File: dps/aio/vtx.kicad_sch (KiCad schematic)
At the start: 14 parts, among them J201 HD VTX, U201 LMR51430YFDDCR

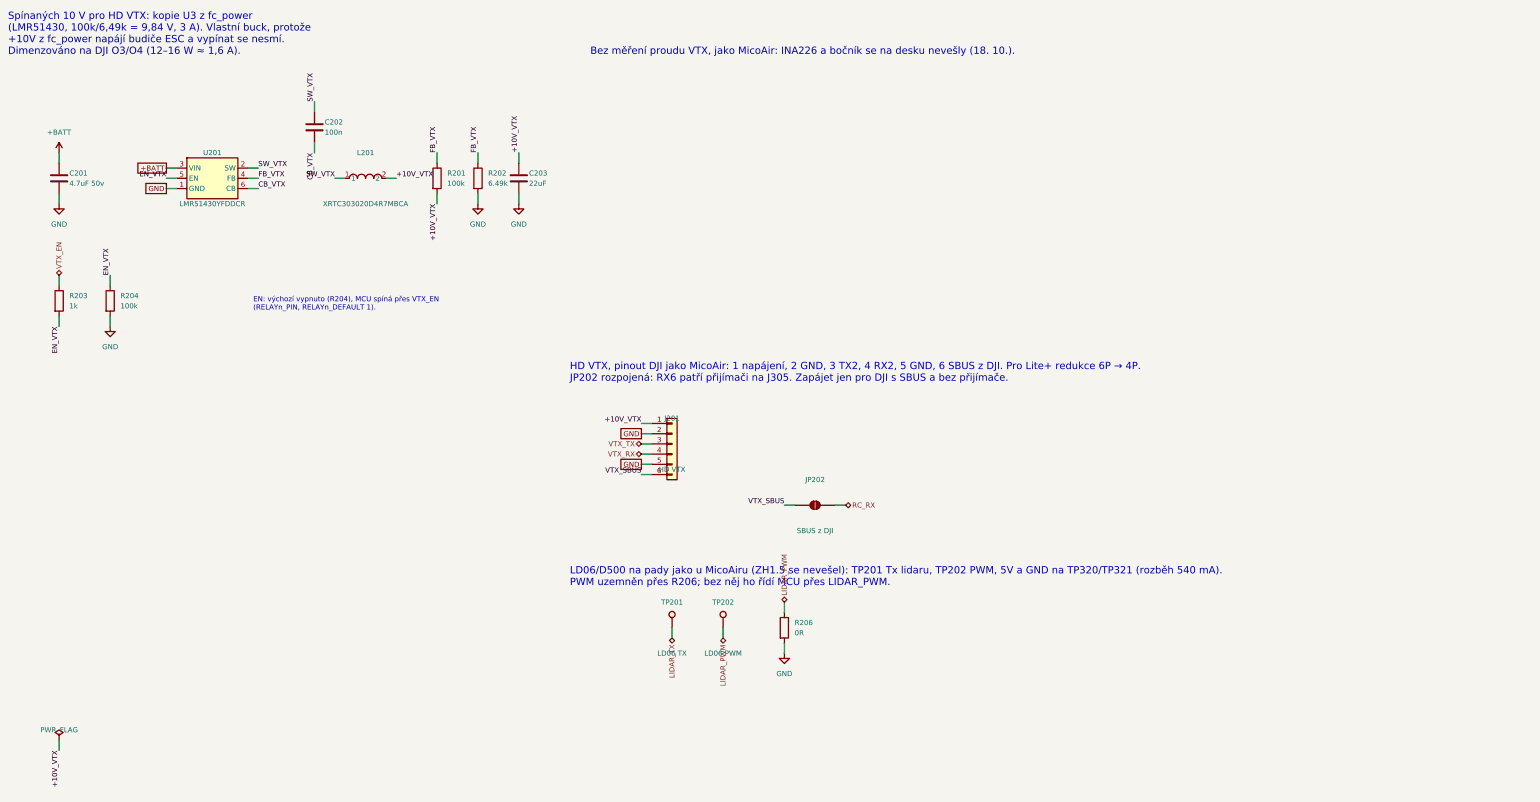
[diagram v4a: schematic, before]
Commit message: feat: fit every AIO part on the board: switch the VTX off +10V and take an ICM-42688-P as the second IMU
The VTX buck and the BMI088 did not fit; the largest free spot was 2.5 x 2.9 mm.
The VTX now hangs on fc_power's +10V behind a TPS22810 load switch (as OpenAIO
feeds it, but switchable), and the second IMU is an ICM-42688-P on OpenAIO's
LGA-14 footprint. The board update now also carries values and LCSC numbers.

Co-Authored-By: Claude Opus 5.5 <noreply@anthropic.com>
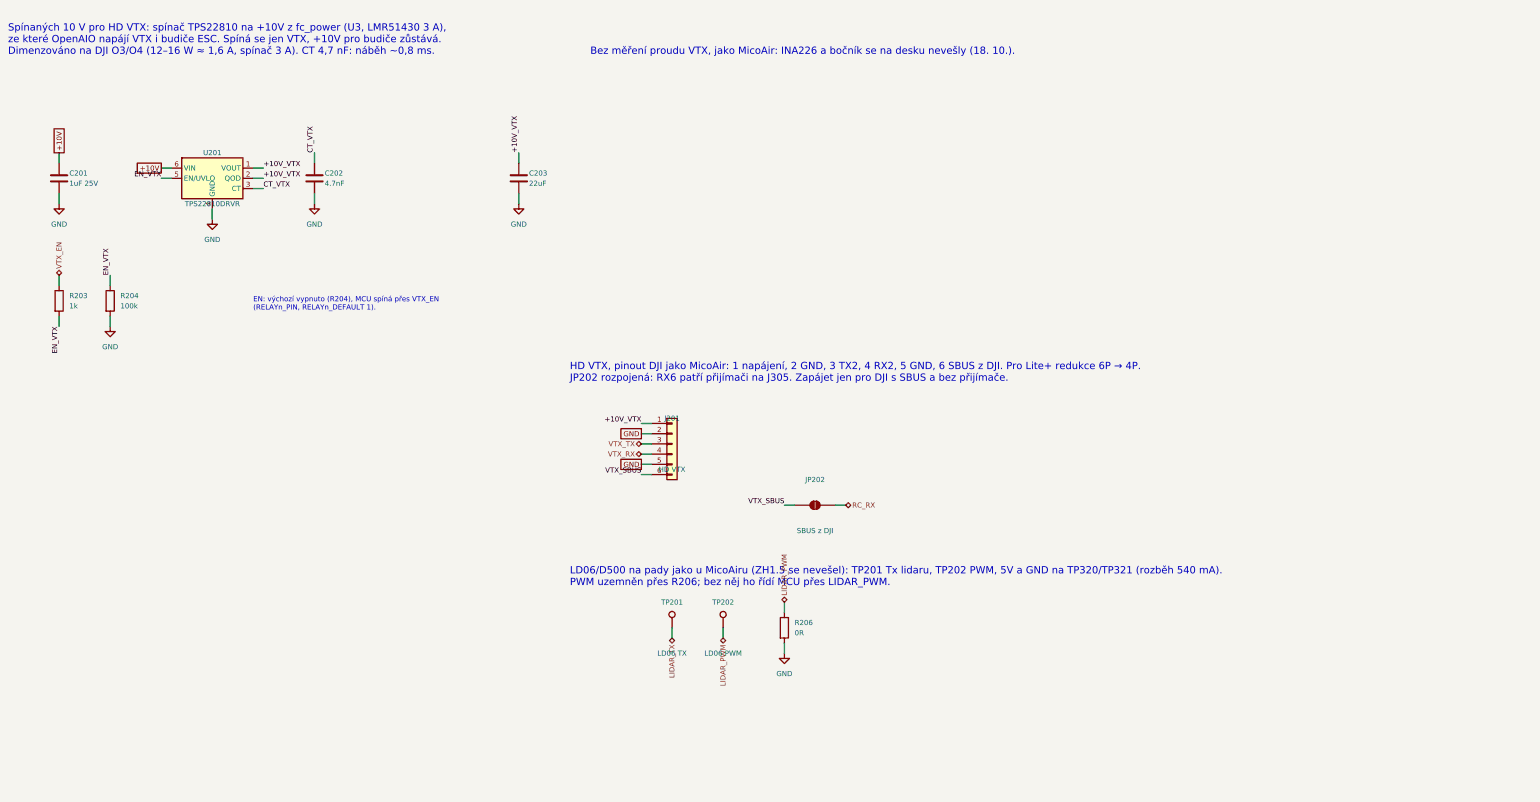
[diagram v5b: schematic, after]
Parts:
- removed L201: XRTC303020D4R7MBCA, lib:IND-SMD_L3.0-W3.0_AFE303020S, symbol lib:XRTC303020D4R7MBCA
- removed R201: 100k, lib:R_0201_0603Metric, symbol lib:R
- removed R202: 6.49k, lib:R_0201_0603Metric, symbol lib:R
- C201: value 4.7uF 50v -> 1uF 25V; footprint lib:C_0805_2012Metric -> lib:C_0402_1005Metric; LCSC C98192 -> (none)
- C202: value 100n -> 4.7nF; LCSC C76939 -> (none)
- U201: value LMR51430YFDDCR -> TPS22810DRVR; footprint lib:SOT-23-6_L2.9-W1.6-P0.95-LS2.9-BL -> lib:WSON-6-1EP_2x2mm_P0.65mm_EP1x1.6mm; symbol lib:LMR51420YDDCR -> Power_Management:TPS22810DRV; LCSC C5219261 -> (none)
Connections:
- net FB_VTX is gone; now on net GND: U201.4 (GND)
- net +10V_VTX: now also U201.1 (VOUT), U201.2 (QOD)
- net GND: now also C202.2, U201.7 (GND); no longer U201.1 (GND)
- net +BATT renamed +10V
- net +10V: now also U201.6 (VIN); no longer U201.3 (VIN)
- removed net CB_VTX: C202.2, U201.6 (CB)
- net SW_VTX renamed CT_VTX
- net CT_VTX: now also U201.3 (CT); no longer U201.2 (SW)
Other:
- note added: "Spínaných 10 V pro HD VTX: spínač TPS22810 na +10V z fc_power (U3, LMR51430 3 A), ze které OpenAIO napájí VTX i budiče ESC. Spíná se jen VTX, +10V pro budiče zůstává. Dimenzováno na DJI O3/O4 (12–16 W ≈ 1,6 A, spínač 3 A). CT 4,7 nF: náběh ~0,8 ms."
- note removed: "Spínaných 10 V pro HD VTX: kopie U3 z fc_power (LMR51430, 100k/6,49k = 9,84 V, 3 A). Vlastní buck, protože +10V z fc_power napájí budiče ESC a vypínat se nesmí. Dimenzováno na DJI O3/O4 (12–16 W ≈ 1,6 A)."
- moved on the sheet: C202, U201

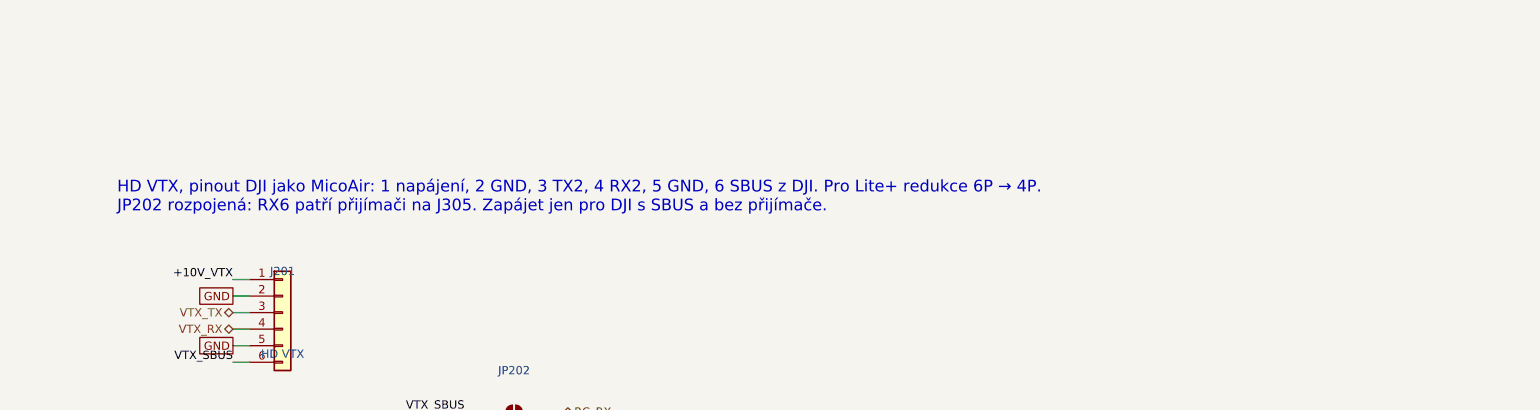
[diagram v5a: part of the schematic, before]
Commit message: feat: route the AIO with its own router after laying it out like MicoAir
The peripherals sat where OpenAIO put them for the RP2354, so about 20 signals
left the H743's BGA on the wrong side. The connectors now sit as on MicoAir,
mirrored, and GPS, receiver, LD06 and both IMUs move to pins whose balls face
them; SERIAL_ORDER keeps the SERIALn numbers. New scripts escape the BGA, clear
OpenAIO leftovers, route in several passes, stitch GND islands and place the
USB-C D+/D- jumpers. 134 of 156 pairs are routed, 22 remain, DRC is clean.

Co-Authored-By: Claude Opus 5.5 <noreply@anthropic.com>
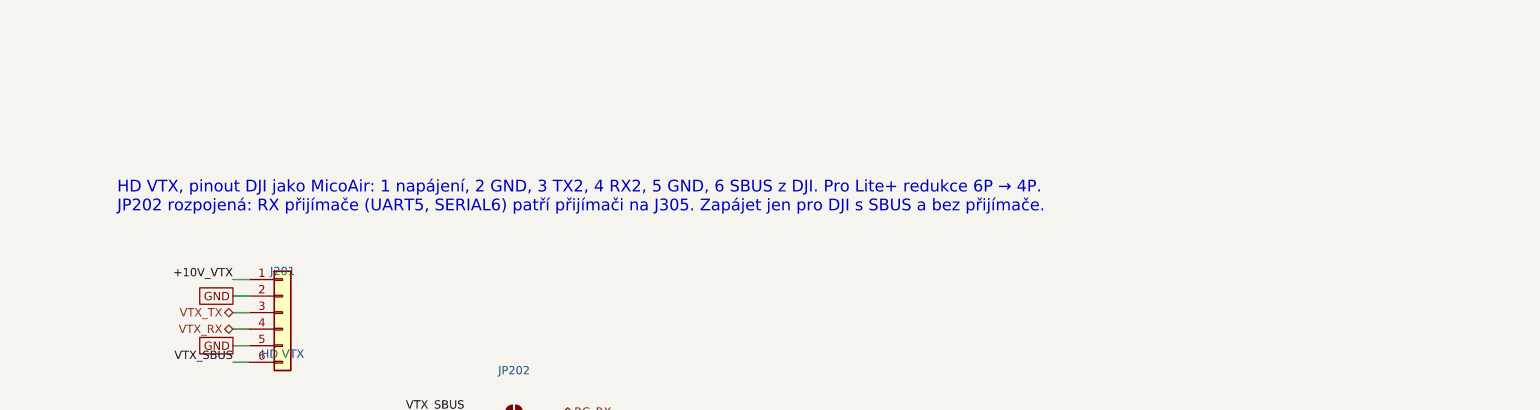
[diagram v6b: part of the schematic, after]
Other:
- note added: "HD VTX, pinout DJI jako MicoAir: 1 napájení, 2 GND, 3 TX2, 4 RX2, 5 GND, 6 SBUS z DJI. Pro Lite+ redukce 6P → 4P. JP202 rozpojená: RX přijímače (UART5, SERIAL6) patří přijímači na J305. Zapájet jen pro DJI s SBUS a bez přijímače."
- note removed: "HD VTX, pinout DJI jako MicoAir: 1 napájení, 2 GND, 3 TX2, 4 RX2, 5 GND, 6 SBUS z DJI. Pro Lite+ redukce 6P → 4P. JP202 rozpojená: RX6 patří přijímači na J305. Zapájet jen pro DJI s SBUS a bez přijímače."
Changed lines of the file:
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@@
 		)
 	)
-	(text "HD VTX, pinout DJI jako MicoAir: 1 napájení, 2 GND, 3 TX2, 4 RX2, 5 GND, 6 SBUS z DJI. Pro Lite+ redukce 6P → 4P.\nJP202 rozpojená: RX6 patří přijímači na J305. Zapájet jen pro DJI s SBUS a bez přijímače."
+	(text "HD VTX, pinout DJI jako MicoAir: 1 napájení, 2 GND, 3 TX2, 4 RX2, 5 GND, 6 SBUS z DJI. Pro Lite+ redukce 6P → 4P.\nJP202 rozpojená: RX přijímače (UART5, SERIAL6) patří přijímači na J305. Zapájet jen pro DJI s SBUS a bez přijímače."
 		(exclude_from_sim no)
 		(at 177.8 101.6 0)
